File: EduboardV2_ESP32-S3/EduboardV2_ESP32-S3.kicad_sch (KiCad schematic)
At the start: 8 parts, among them J1 EduboardV2 PCIE UP Board Conn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, SW1 K2-1102SP-C4SC-04, SW2 K2-1102SP-C4SC-04, U1 ESP32-S3-WROOM-1(N8R2)

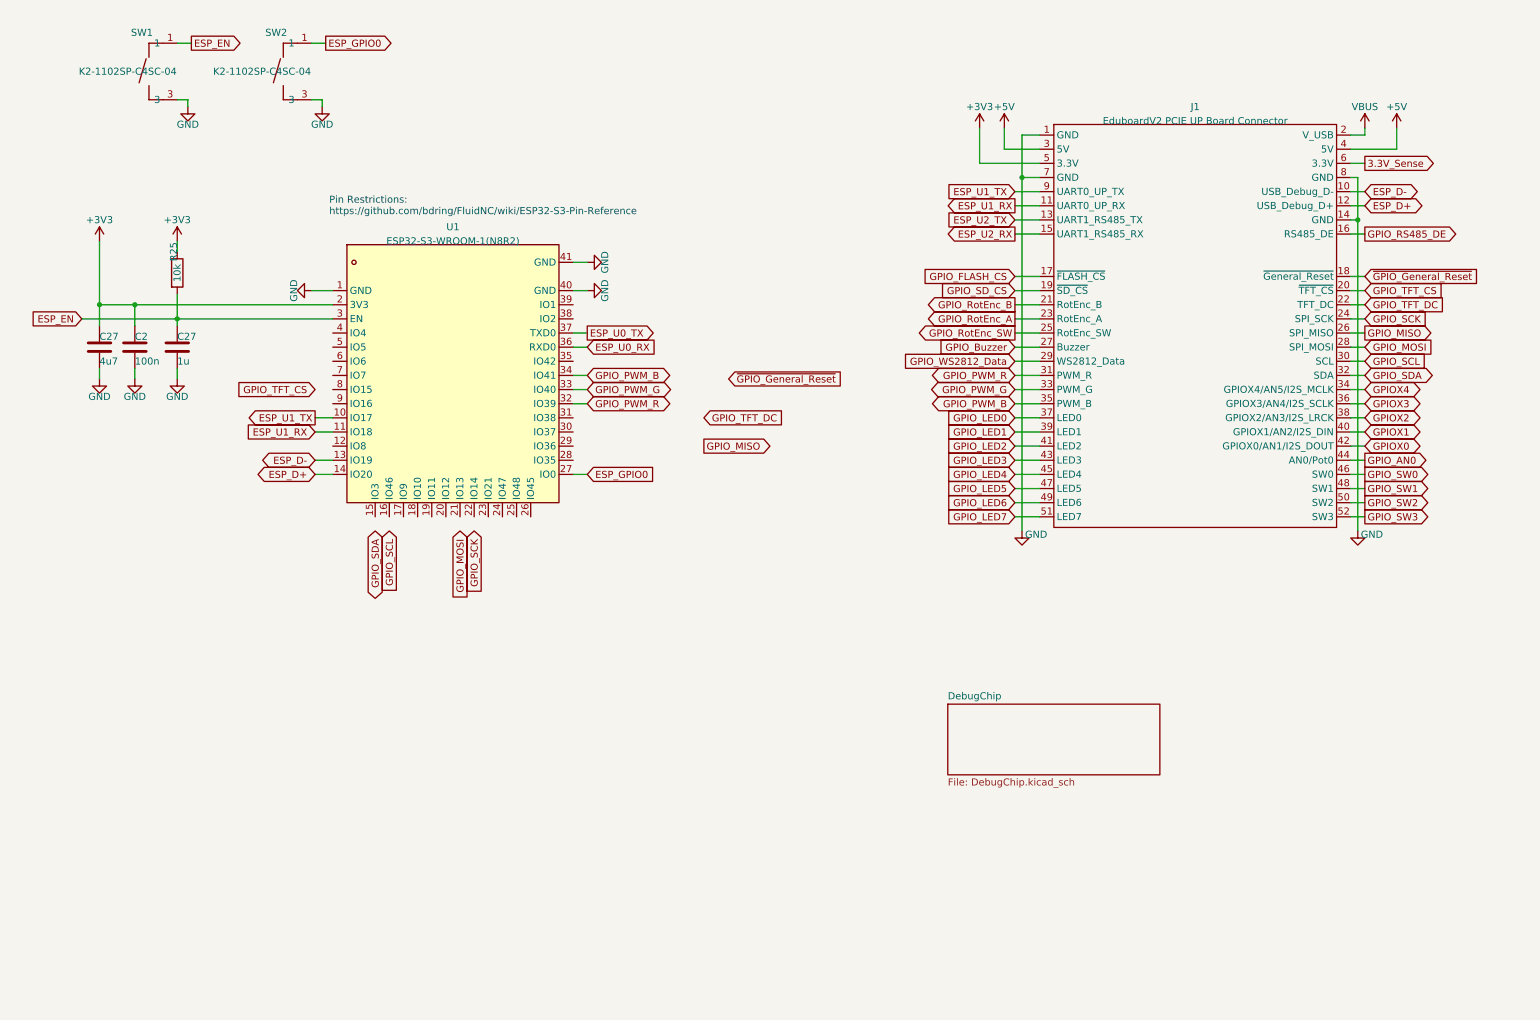
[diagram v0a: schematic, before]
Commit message: distribute signals to pins
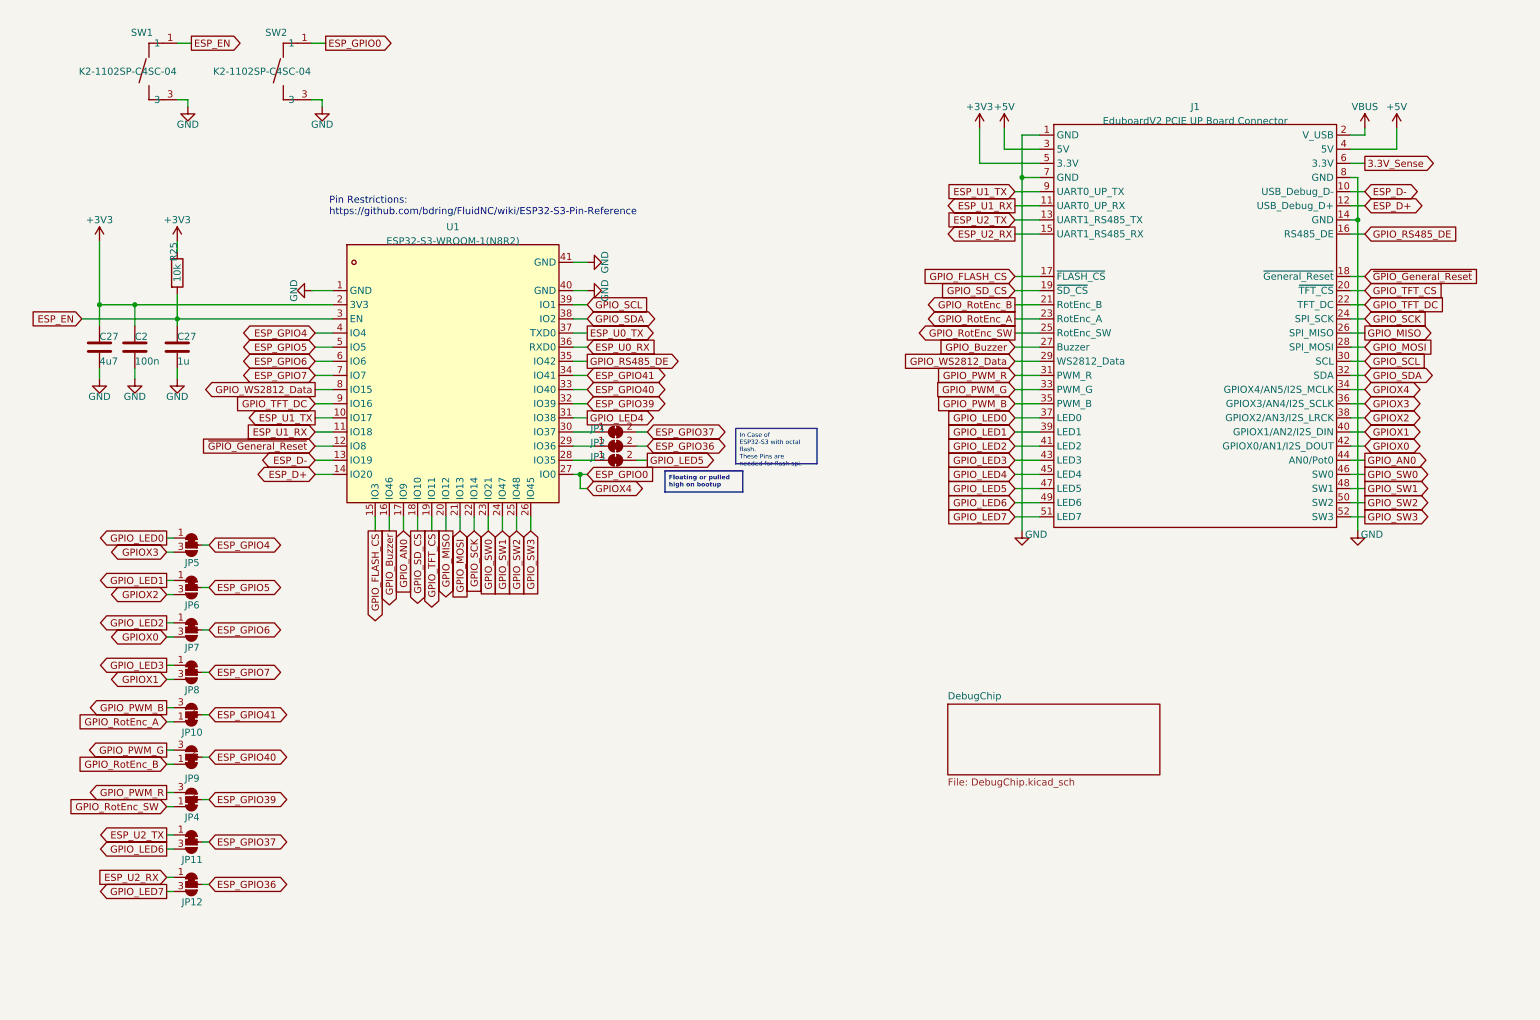
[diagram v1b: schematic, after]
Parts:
- added JP1, JP2, JP3: SolderJumper_2_Bridged, symbol Jumper:SolderJumper_2_Bridged
- added JP10, JP11, JP12, JP4, JP5, JP6, JP7, JP8, JP9: SolderJumper_3_Bridged12, EduboardV2_kicadlib:SolderJumper_Small-3_bridged12, symbol EduboardV2_Kicadlib:SolderJumper_Small_3_Bridged12
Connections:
- net GPIOX4 is gone; now on net ESP_GPIO0: J1.34 (GPIOX4/AN5/I2S_MCLK)
- net ESP_U2_RX: now also JP12.1 (A)
- net ESP_U2_TX: now also JP11.1 (A)
- net GPIOX0: now also JP7.3 (B)
- net GPIOX1: now also JP8.3 (B)
- net GPIOX2: now also JP6.3 (B)
- net GPIOX3: now also JP5.3 (B)
- net GPIO_AN0: now also U1.17 (IO9)
- net GPIO_Buzzer: now also U1.16 (IO46)
- net GPIO_FLASH_CS: now also U1.15 (IO3)
- net GPIO_LED0: now also JP5.1 (A)
- net GPIO_LED1: now also JP6.1 (A)
- net GPIO_LED2: now also JP7.1 (A)
- net GPIO_LED3: now also JP8.1 (A)
- net GPIO_LED4: now also U1.31 (IO38)
- net GPIO_LED5: now also JP3.2 (B)
- net GPIO_LED6: now also JP11.3 (B)
- net GPIO_LED7: now also JP12.3 (B)
- net GPIO_MISO: now also U1.20 (IO12)
- net GPIO_MOSI: now also U1.21 (IO13)
- net GPIO_PWM_B: now also JP10.3 (B); no longer U1.34 (IO41)
- net GPIO_PWM_G: now also JP9.3 (B); no longer U1.33 (IO40)
- net GPIO_PWM_R: now also JP4.3 (B); no longer U1.32 (IO39)
- net GPIO_RS485_DE: now also U1.35 (IO42)
- net GPIO_RotEnc_A: now also JP10.1 (A)
- net GPIO_RotEnc_B: now also JP9.1 (A)
- net GPIO_RotEnc_SW: now also JP4.1 (A)
- net GPIO_SCK: now also U1.22 (IO14)
- net GPIO_SCL: now also U1.39 (IO1)
- net GPIO_SDA: now also U1.38 (IO2)
- net GPIO_SD_CS: now also U1.18 (IO10)
- net GPIO_SW0: now also U1.23 (IO21)
- net GPIO_SW1: now also U1.24 (IO47)
- net GPIO_SW2: now also U1.25 (IO48)
- net GPIO_SW3: now also U1.26 (IO45)
- net GPIO_TFT_CS: now also U1.19 (IO11)
- net GPIO_TFT_DC: now also U1.9 (IO16)
- net GPIO_WS2812_Data: now also U1.8 (IO15)
- net ~{GPIO_General_Reset}: now also U1.12 (IO8)
- net at U1.28 (IO35): now also JP3.1 (A)
- net at U1.29 (IO36): now also JP2.1 (A)
- net at U1.30 (IO37): now also JP1.1 (A)
- net ESP_GPIO4: now reaches U1.4 (IO4)
- net ESP_GPIO4: now also JP5.2 (C)
- net ESP_GPIO5: now reaches U1.5 (IO5)
- net ESP_GPIO5: now also JP6.2 (C)
- net ESP_GPIO6: now reaches U1.6 (IO6)
- net ESP_GPIO6: now also JP7.2 (C)
- net ESP_GPIO7: now reaches U1.7 (IO7)
- net ESP_GPIO7: now also JP8.2 (C)
- new net ESP_GPIO36: JP12.2 (C), JP2.2 (B)
- new net ESP_GPIO37: JP1.2 (B), JP11.2 (C)
- new net ESP_GPIO39: JP4.2 (C), U1.32 (IO39)
- new net ESP_GPIO40: JP9.2 (C), U1.33 (IO40)
- new net ESP_GPIO41: JP10.2 (C), U1.34 (IO41)

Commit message: finish schematic. Do Layout
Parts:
- C27: JLCPCB Part # (none) -> C77083; LCSC Part (none) -> C77083
- JP1, JP2, JP3: footprint (none) -> Jumper:SolderJumper-2_P1.3mm_Bridged_RoundedPad1.0x1.5mm
- R25: footprint Resistor_SMD:R_0603_1608Metric -> Resistor_SMD:R_0402_1005Metric; JLCPCB Part # (none) -> C71617; LCSC Part (none) -> C71617
- SW1, SW2: JLCPCB Part # (none) -> C127509
- U1: JLCPCB Part # (none) -> C2913204
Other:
- moved on the sheet: C2, C27, JP1, JP10, JP11, JP12, JP2, JP3, JP4, JP5, JP6, JP7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

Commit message: add jumper description on board
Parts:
- JP11, JP12: footprint EduboardV2_kicadlib:SolderJumper_Small-3_bridged12 -> EduboardV2_kicadlib:SolderJumper_Small-3_bridged23; symbol EduboardV2_Kicadlib:SolderJumper_Small_3_Bridged12 -> EduboardV2_Kicadlib:SolderJumper_Small_3_Bridged23
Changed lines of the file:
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@@
     )
   )
-  (symbol (lib_id "EduboardV2_Kicadlib:SolderJumper_Small_3_Bridged12") (at 38.1 184.15 0) (unit 1)
+  (symbol (lib_id "EduboardV2_Kicadlib:SolderJumper_Small_3_Bridged23") (at 38.1 184.15 0) (unit 1)
     (in_bom yes) (on_board yes) (dnp no)
     (property "Reference" "JP11" (at 38.227 187.325 0)
@@
       (effects (font (size 1.27 1.27)) hide)
     )
-    (property "Footprint" "EduboardV2_kicadlib:SolderJumper_Small-3_bridged12" (at 37.465 191.135 0)
+    (property "Footprint" "EduboardV2_kicadlib:SolderJumper_Small-3_bridged23" (at 37.465 191.135 0)
       (effects (font (size 1.27 1.27)) hide)
     )
@@
     )
   )
-  (symbol (lib_id "EduboardV2_Kicadlib:SolderJumper_Small_3_Bridged12") (at 38.1 191.77 0) (unit 1)
+  (symbol (lib_id "EduboardV2_Kicadlib:SolderJumper_Small_3_Bridged23") (at 38.1 191.77 0) (unit 1)
     (in_bom yes) (on_board yes) (dnp no)
     (property "Reference" "JP12" (at 38.227 194.945 0)
@@
       (effects (font (size 1.27 1.27)) hide)
     )
-    (property "Footprint" "EduboardV2_kicadlib:SolderJumper_Small-3_bridged12" (at 37.465 198.755 0)
+    (property "Footprint" "EduboardV2_kicadlib:SolderJumper_Small-3_bridged23" (at 37.465 198.755 0)
       (effects (font (size 1.27 1.27)) hide)
     )

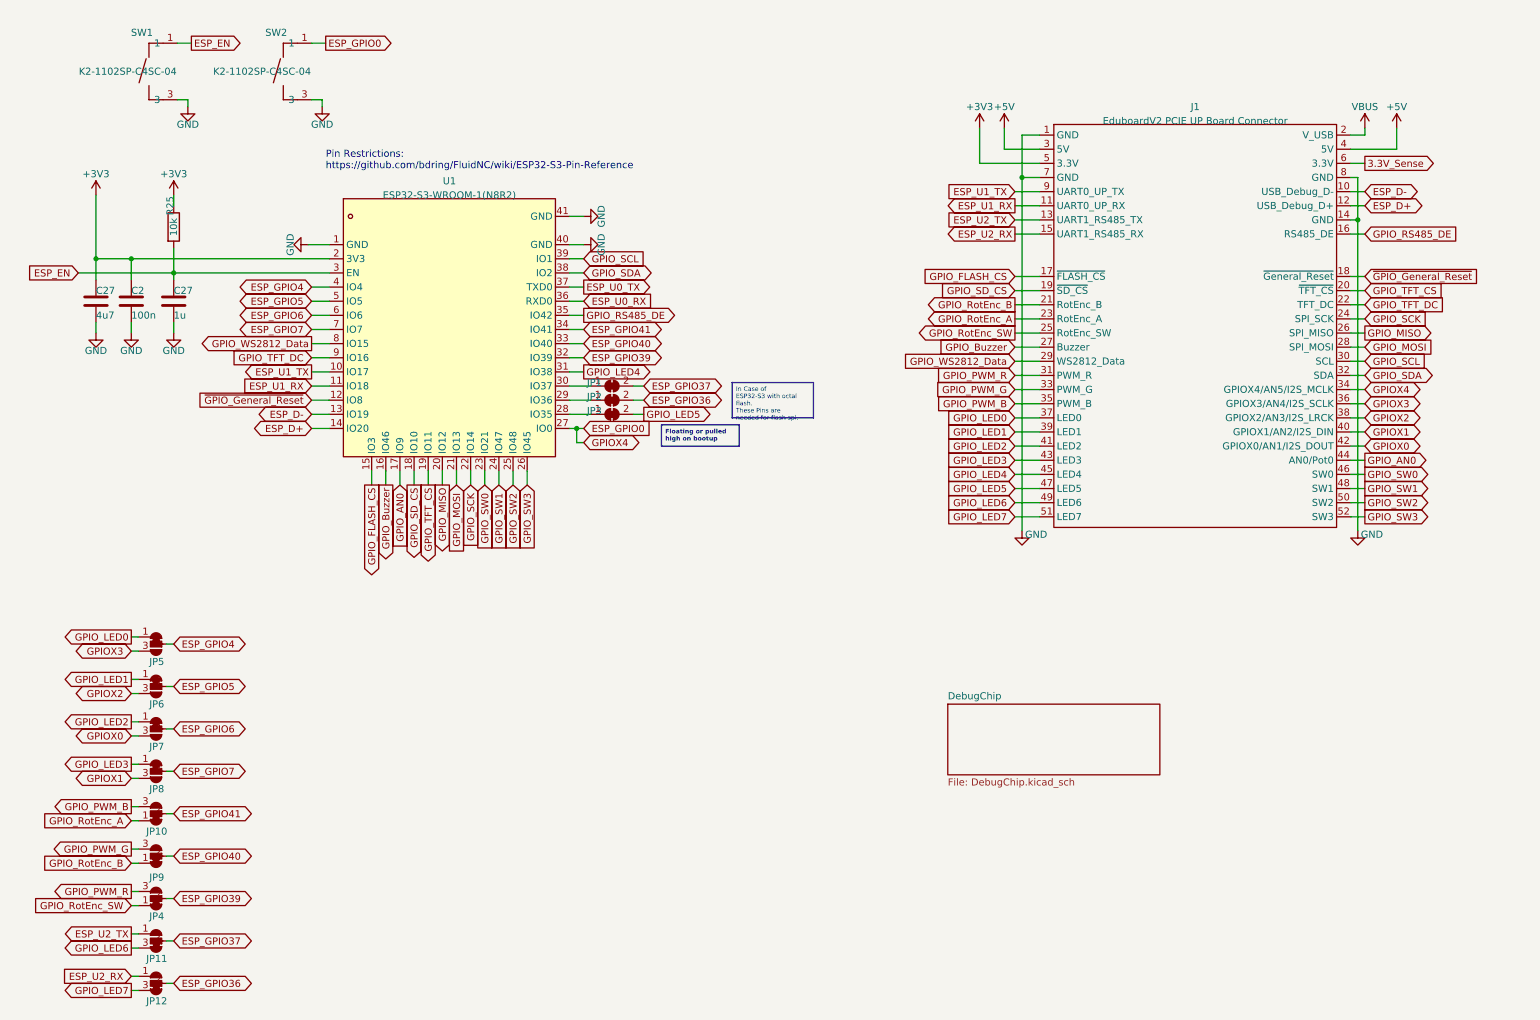
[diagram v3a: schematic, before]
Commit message: Do all modifications for V1.1 and create production data
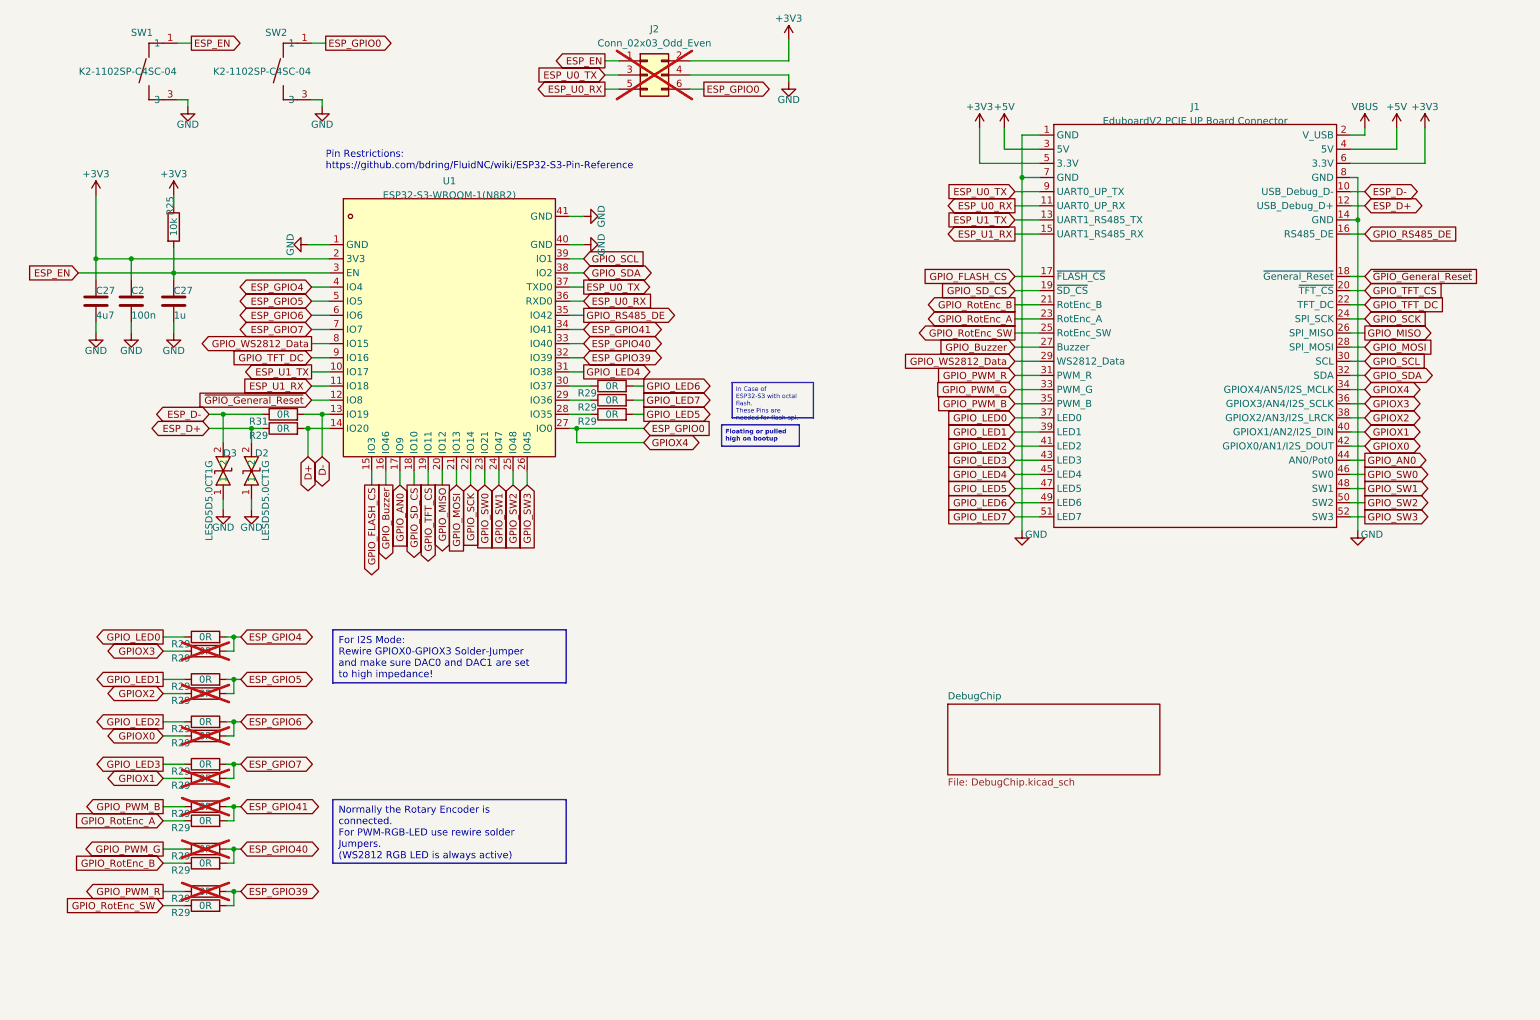
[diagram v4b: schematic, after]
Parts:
- removed JP1, JP2, JP3: SolderJumper_2_Bridged, Jumper:SolderJumper-2_P1.3mm_Bridged_RoundedPad1.0x1.5mm, symbol Jumper:SolderJumper_2_Bridged
- removed JP10, JP4, JP5, JP6, JP7, JP8, JP9: SolderJumper_3_Bridged12, EduboardV2_kicadlib:SolderJumper_Small-3_bridged12, symbol EduboardV2_Kicadlib:SolderJumper_Small_3_Bridged12
- removed JP11, JP12: SolderJumper_3_Bridged12, EduboardV2_kicadlib:SolderJumper_Small-3_bridged23, symbol EduboardV2_Kicadlib:SolderJumper_Small_3_Bridged23
- added D2, D3: LESD5D5.0CT1G, EduboardV2_kicadlib:SOD-523_L1.2-W0.8-LS1.6-BI, symbol EduboardV2_kicadlib:LESD5D5.0CT1G
- added J2: Conn_02x03_Odd_Even, Connector_PinHeader_2.54mm:PinHeader_2x03_P2.54mm_Vertical, symbol Connector_Generic:Conn_02x03_Odd_Even
- added R29 (x18), R31: 0R, Resistor_SMD:R_0603_1608Metric, symbol Device:R
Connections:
- net 3.3V_Sense is gone; now on net +3V3: J1.6 (3.3V)
- net ESP_U2_RX is gone; now on net ESP_U1_RX: J1.15 (UART1_RS485_RX)
- net ESP_U2_TX is gone; now on net ESP_U1_TX: J1.13 (UART1_RS485_TX)
- net +3V3: now also J2.2 (Pin_2)
- net ESP_D+: now also D2.2, R29.1; no longer U1.14 (IO20)
- net ESP_D-: now also D3.2, R31.1; no longer U1.13 (IO19)
- net ESP_EN: now also J2.1 (Pin_1)
- net ESP_GPIO0: now also J2.6 (Pin_6)
- net ESP_GPIO39: now also R29.2, R29.2
- net ESP_GPIO4: now also R29.2, R29.2
- net ESP_GPIO40: now also R29.2, R29.2
- net ESP_GPIO41: now also R29.2, R29.2
- net ESP_GPIO5: now also R29.2, R29.2
- net ESP_GPIO6: now also R29.2, R29.2
- net ESP_GPIO7: now also R29.2, R29.2
- net ESP_U0_RX: now also J1.11 (UART0_UP_RX), J2.5 (Pin_5)
- net ESP_U0_TX: now also J1.9 (UART0_UP_TX), J2.3 (Pin_3)
- net ESP_U1_RX: no longer J1.11 (UART0_UP_RX)
- net ESP_U1_TX: no longer J1.9 (UART0_UP_TX)
- net GND: now also D2.1, D3.1, J2.4 (Pin_4)
- net GPIOX0: now also R29.1
- net GPIOX1: now also R29.1
- net GPIOX2: now also R29.1
- net GPIOX3: now also R29.1
- net GPIO_LED0: now also R29.1
- net GPIO_LED1: now also R29.1
- net GPIO_LED2: now also R29.1
- net GPIO_LED3: now also R29.1
- net GPIO_LED5: now also R29.2
- net GPIO_LED6: now also R29.2
- net GPIO_LED7: now also R29.2
- net GPIO_PWM_B: now also R29.1
- net GPIO_PWM_G: now also R29.1
- net GPIO_PWM_R: now also R29.1
- net GPIO_RotEnc_A: now also R29.1
- net GPIO_RotEnc_B: now also R29.1
- net GPIO_RotEnc_SW: now also R29.1
- net at U1.29 (IO36): now also R29.1
- net at U1.30 (IO37): now also R29.1
- net at U1.28 (IO35): now also R29.1
- new net D+: R29.2, U1.14 (IO20)
- new net D-: R31.2, U1.13 (IO19)

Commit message: migrate to kicad v8.
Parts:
- renumbered C27 to C1, C27 to C3, D3 to D1, R25 to R1, R29 to R10, R29 to R11, R29 to R12, R29 to R13, R29 to R14, R29 to R15, R31 to R16, R29 to R17, R29 to R18, R29 to R19, R29 to R2, R29 to R20, R29 to R3, R29 to R4, R29 to R5, R29 to R6, R29 to R7, R29 to R8, R29 to R9
